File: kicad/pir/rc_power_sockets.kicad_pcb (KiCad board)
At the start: 2 copper layers, 50 x 50 mm, 32 parts, among them IC1 ATTINY85, J1 PIR, J2 433MHZ, J3 433MHZ, P1 ICSP, P2 ALT_PWR, Q1 NMOS, Q2 PMOS, SW1 SWITCH_INV, U1 MCP1755ST-3302E/DB

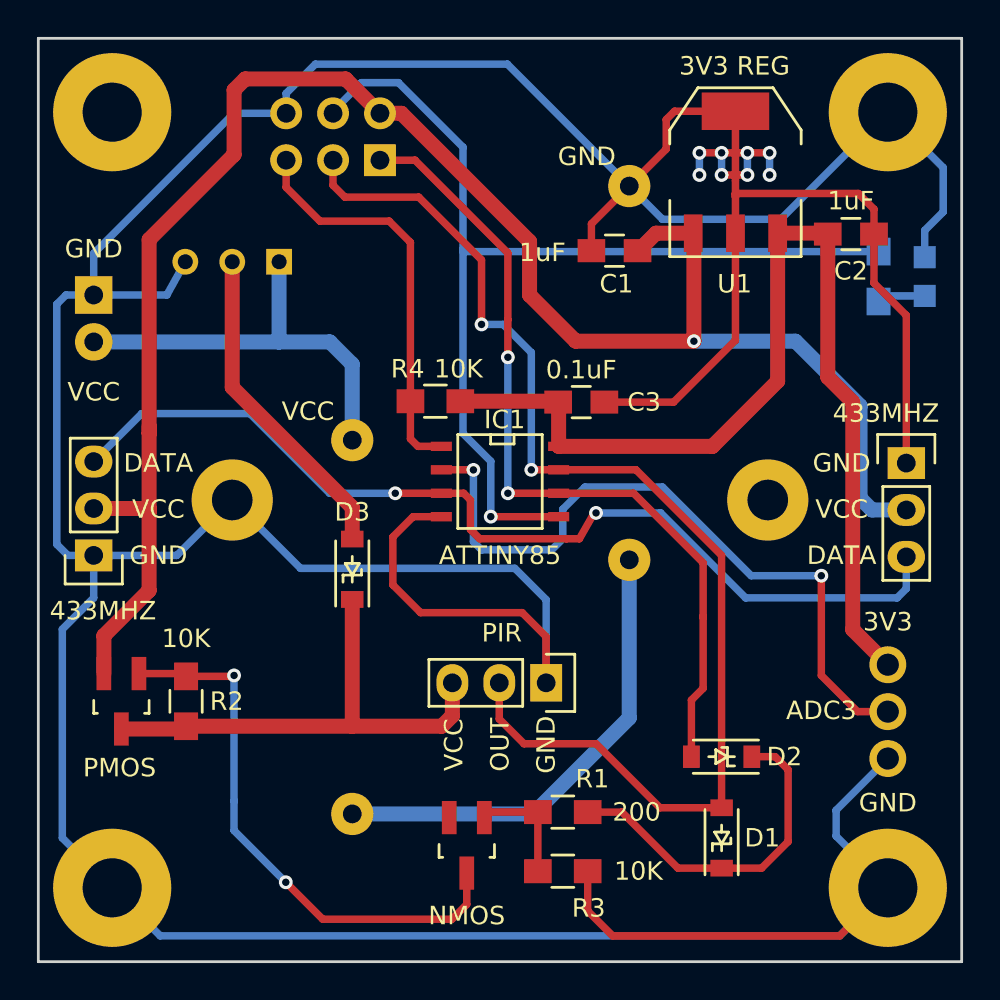
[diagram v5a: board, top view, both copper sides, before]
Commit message: switch_power trace tweak
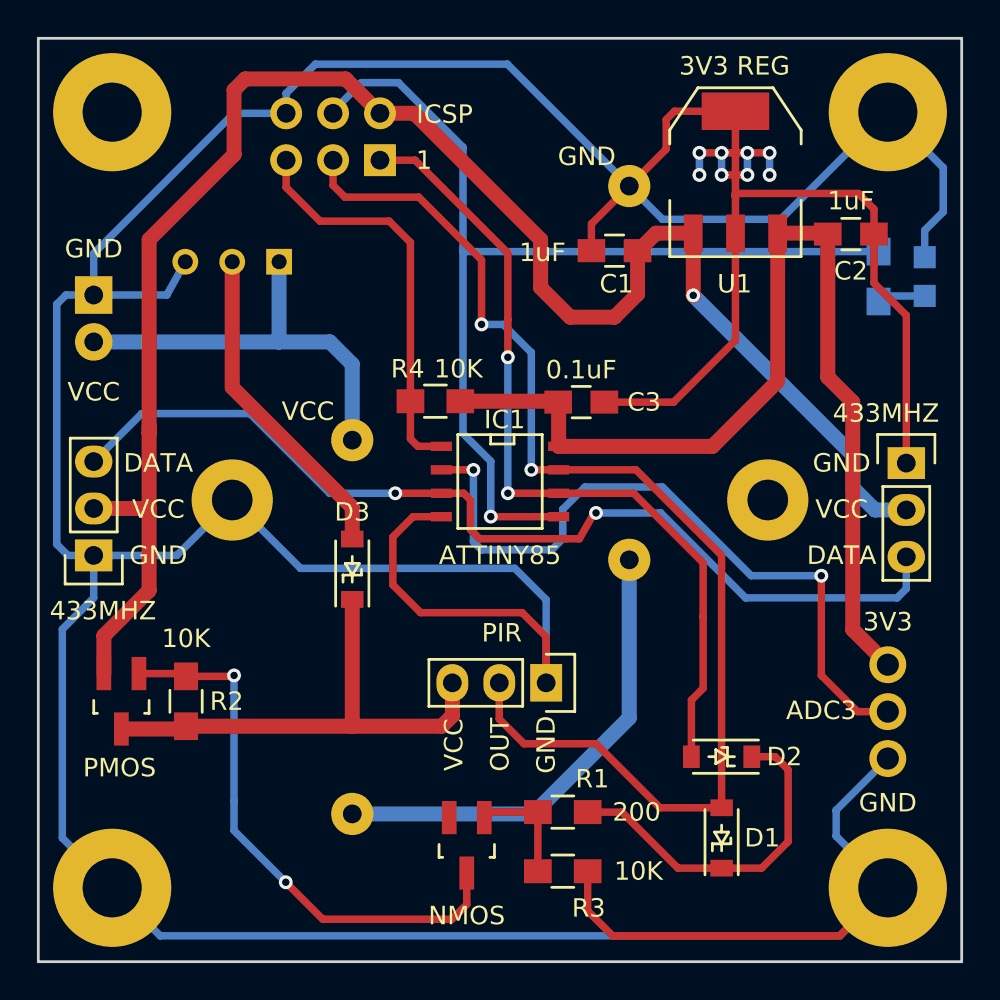
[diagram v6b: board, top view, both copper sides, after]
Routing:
- net /SWITCH_POWER: track 98.8 -> 94.6 mm
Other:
- board text added: "ICSP"
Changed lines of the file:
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@@
     (links 58)
     (no_connects 0)
-    (area 119.924999 59.924999 170.075001 110.075001)
+    (area 117.425 58.475 171.675 111.375)
     (thickness 1.6)
-    (drawings 45)
-    (tracks 280)
+    (drawings 47)
+    (tracks 282)
     (zones 0)
     (modules 32)
@@
       (rotate (xyz 0 0 0))
     )
+  )
+  (gr_text ICSP (at 142.0028 64.1152) (layer F.SilkS)
+    (effects (font (size 1 1) (thickness 0.15)))
+  )
+  (gr_text 1 (at 140.8852 66.6044) (layer F.SilkS)
+    (effects (font (size 1 1) (thickness 0.15)))
   )
   (gr_text VCC (at 123 79) (layer B.SilkS)
@@
   (segment (start 144 87.7) (end 147.8 87.7) (width 0.406) (layer B.Cu) (net 7))
   (segment (start 143.56 87.26) (end 144 87.7) (width 0.406) (layer B.Cu) (net 7))
+  (segment (start 155.464 70.552) (end 155.464 73.9188) (width 0.813) (layer F.Cu) (net 8))
+  (segment (start 165.3072 85.54) (end 167 85.54) (width 0.813) (layer B.Cu) (net 8))
+  (segment (start 164.1008 84.3336) (end 165.3072 85.54) (width 0.813) (layer B.Cu) (net 8))
+  (segment (start 164.1008 82.5556) (end 164.1008 84.3336) (width 0.813) (layer B.Cu) (net 8))
+  (segment (start 155.4648 73.9196) (end 164.1008 82.5556) (width 0.813) (layer B.Cu) (net 8))
+  (via (at 155.4648 73.9196) (size 0.75) (drill 0.4) (layers F.Cu B.Cu) (net 8))
+  (segment (start 155.464 73.9188) (end 155.4648 73.9196) (width 0.813) (layer F.Cu) (net 8))
+  (segment (start 138.5 64.06) (end 140.36 64.06) (width 0.813) (layer F.Cu) (net 8))
+  (segment (start 152.45 73.85) (end 152.45 71.5) (width 0.813) (layer F.Cu) (net 8))
+  (segment (start 151.2 75.1) (end 152.45 73.85) (width 0.813) (layer F.Cu) (net 8))
+  (segment (start 148.8 75.1) (end 151.2 75.1) (width 0.813) (layer F.Cu) (net 8))
+  (segment (start 147.2 73.5) (end 148.8 75.1) (width 0.813) (layer F.Cu) (net 8))
+  (segment (start 147.2 70.9) (end 147.2 73.5) (width 0.813) (layer F.Cu) (net 8))
+  (segment (start 140.36 64.06) (end 147.2 70.9) (width 0.813) (layer F.Cu) (net 8))
   (segment (start 152.45 71.5) (end 152.5 71.5) (width 0.813) (layer F.Cu) (net 8))
   (segment (start 152.5 71.5) (end 153.448 70.552) (width 0.813) (layer F.Cu) (net 8))
   (segment (start 153.448 70.552) (end 155.464 70.552) (width 0.813) (layer F.Cu) (net 8))
-  (segment (start 155.5 76.4) (end 155.5 70.588) (width 0.813) (layer F.Cu) (net 8))
   (segment (start 155.5 70.588) (end 155.464 70.552) (width 0.813) (layer F.Cu) (net 8))
-  (segment (start 146.6 71) (end 146.6 73.9) (width 0.813) (layer F.Cu) (net 8))
-  (segment (start 138.5 64.06) (end 139.66 64.06) (width 0.813) (layer F.Cu) (net 8))
-  (segment (start 146.6 71) (end 139.66 64.06) (width 0.813) (layer F.Cu) (net 8))
-  (segment (start 165.14 85.54) (end 167 85.54) (width 0.813) (layer B.Cu) (net 8))
-  (segment (start 165.14 85.54) (end 164.5 84.9) (width 0.813) (layer B.Cu) (net 8))
-  (segment (start 164.5 84.9) (end 164.5 79.9) (width 0.813) (layer B.Cu) (net 8))
-  (segment (start 164.5 79.9) (end 161 76.4) (width 0.813) (layer B.Cu) (net 8))
-  (segment (start 161 76.4) (end 155.5 76.4) (width 0.813) (layer B.Cu) (net 8))
-  (via (at 155.5 76.4) (size 0.75) (drill 0.4) (layers F.Cu B.Cu) (net 8))
-  (segment (start 149.1 76.4) (end 155.5 76.4) (width 0.813) (layer F.Cu) (net 8))
-  (segment (start 146.6 73.9) (end 149.1 76.4) (width 0.813) (layer F.Cu) (net 8))
   (segment (start 126 85.46) (end 126 89.9) (width 0.813) (layer F.Cu) (net 8))
   (segment (start 123.55 92.35) (end 123.55 94.39886) (width 0.813) (layer F.Cu) (net 8))

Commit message: Flipped the radio connector to the back
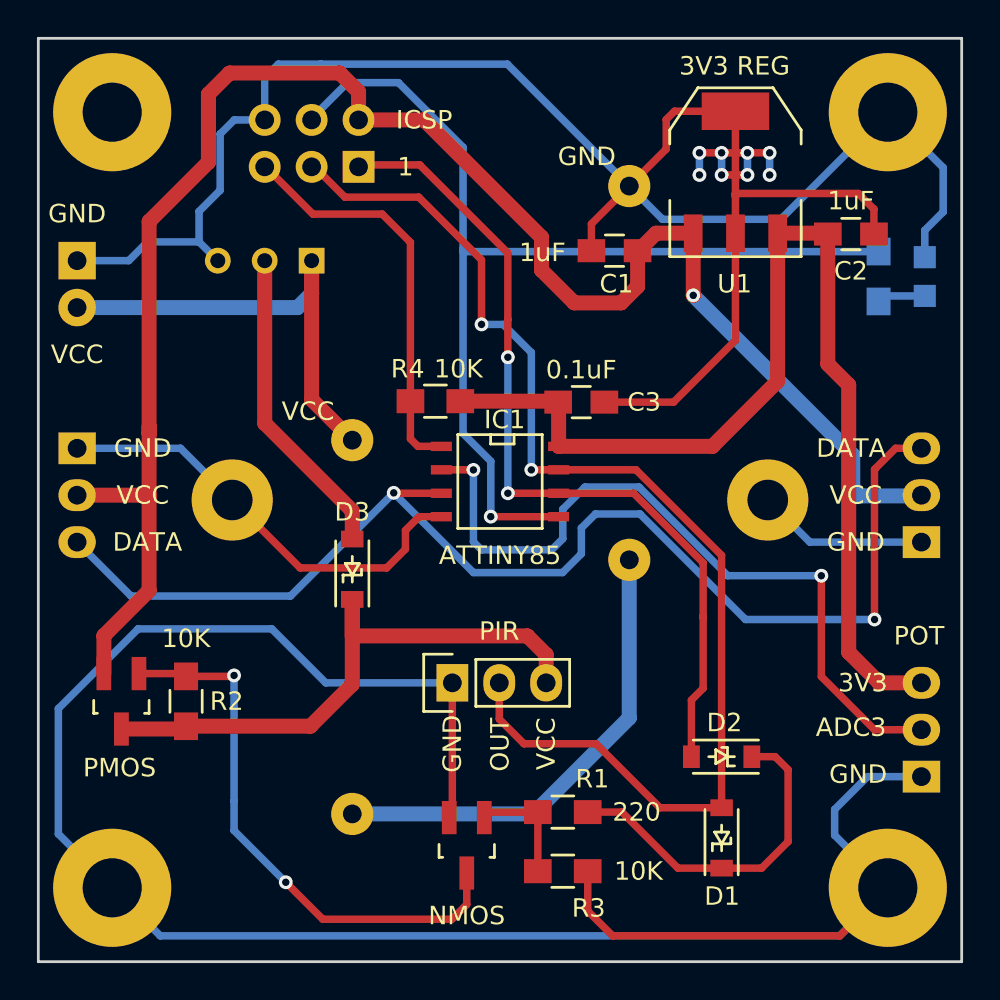
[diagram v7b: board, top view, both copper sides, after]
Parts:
- J2, J3: moved to B.Cu
- R1: value 200 -> 220
- RV1: footprint Potentiometers:Potentiometer_WirePads_Small -> Pin_Headers:Pin_Header_Straight_1x03
- moved J2 5.87 mm to (122.1, 82.2), turned to 270 degrees
- moved J1 5.08 mm to (142.4, 94.9), turned to 0 degrees
- moved J3 4.36 mm to (167.8, 87.3), turned to 90 degrees
- moved RV1 2.07 mm to (167.8, 100.0)
- moved P2 2.07 mm to (122.1, 72.0)
- moved SW1 1.76 mm to (132.3, 72.0)
- moved REF** 1.34 mm to (159.8, 89.6)
- moved P1 1.21 mm to (137.3, 67.0)
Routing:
- net GND: track 301.1 -> 275.8 mm
- net /RADIO_DATA: track 54.4 -> 66.7 mm
- net /POWER: track 27.2 -> 32.5 mm
- net /3.3v: track 56.3 -> 59.3 mm
- net VCC: track 23.0 -> 25.4 mm
- net /ADC3: track 38.8 -> 41.1 mm
- net /MOSI: track 56.2 -> 57.6 mm
- net /SWITCH_POWER: track 94.6 -> 95.9 mm
- net /MISO: track 45.0 -> 46.1 mm
- net /VCC_SWITCHED: track 17.7 -> 17.0 mm
- net /SCK: track 66.1 -> 66.7 mm
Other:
- board text added: "POT"

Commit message: Easier hand soldering
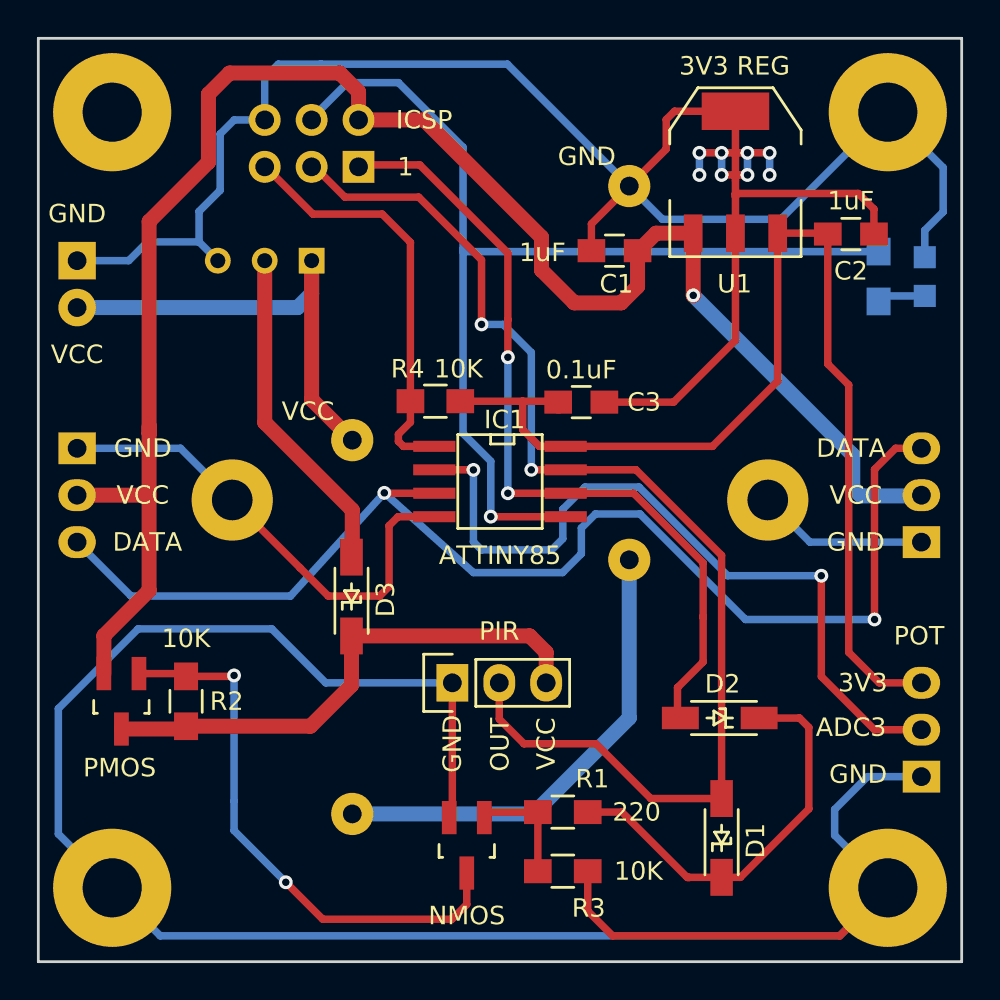
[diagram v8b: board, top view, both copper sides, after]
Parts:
- D2: footprint theapi_footprints:SOD-123-Schottky -> SOD-123-Schottky
- IC1: footprint SMD_Packages:SOIC-8-N -> SOIC-8-N-hand-sold
- moved D2 2.10 mm to (156.9, 96.8)
- moved D3 1.48 mm to (137.0, 90.2)
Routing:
- net /POWER: track 32.5 -> 28.7 mm
- net /NBASE_ON: track 18.9 -> 22.3 mm
- net GND: track 275.8 -> 278.4 mm
- net /3.3v: track 59.3 -> 61.5 mm
- net /MISO: track 46.1 -> 44.2 mm
- net /RESET: track 22.3 -> 24.1 mm
- net /RADIO_DATA: track 66.7 -> 67.3 mm
